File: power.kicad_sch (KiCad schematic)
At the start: 45 parts, among them J501 PJ-002AH-SMT-TR, Q501 SI2369DS-T1-BE3, U501 TPS5402, U502 TLV1117-50, U503 MIC5317-3.3YM5-TR

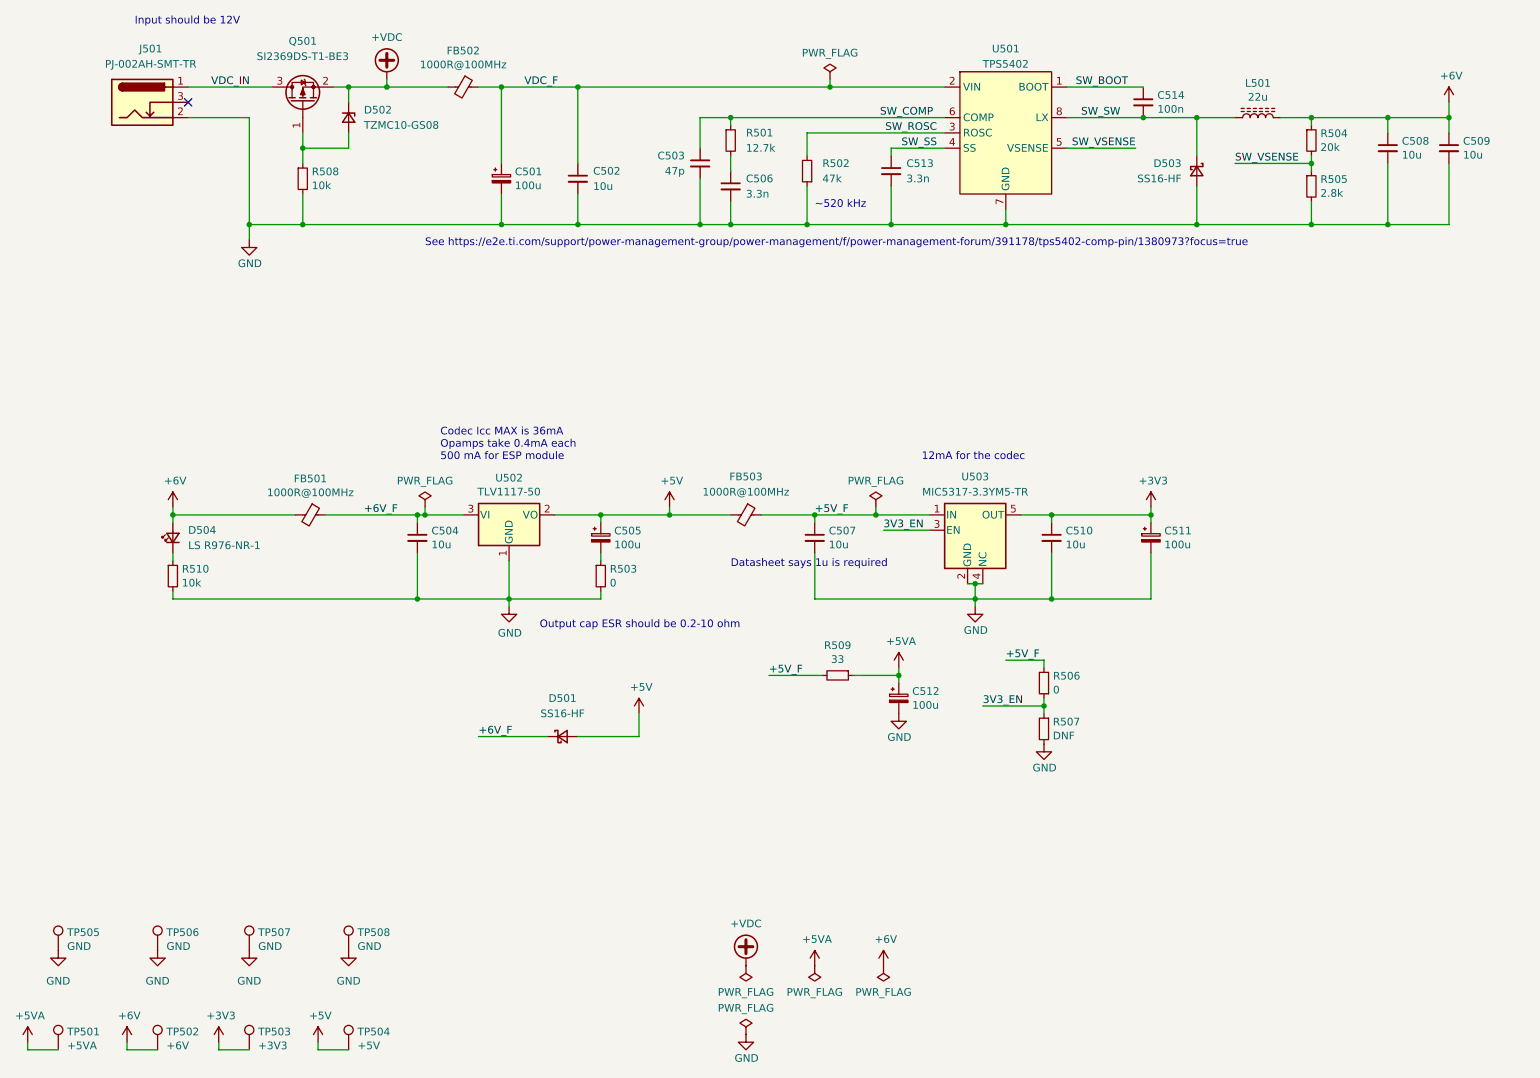
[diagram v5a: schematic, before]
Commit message: Resolve some issues
- Add missing MIDI connector pins to symbol
- Isolate low-ESR capacitors from 1117
- Fix DRC errors in footprints
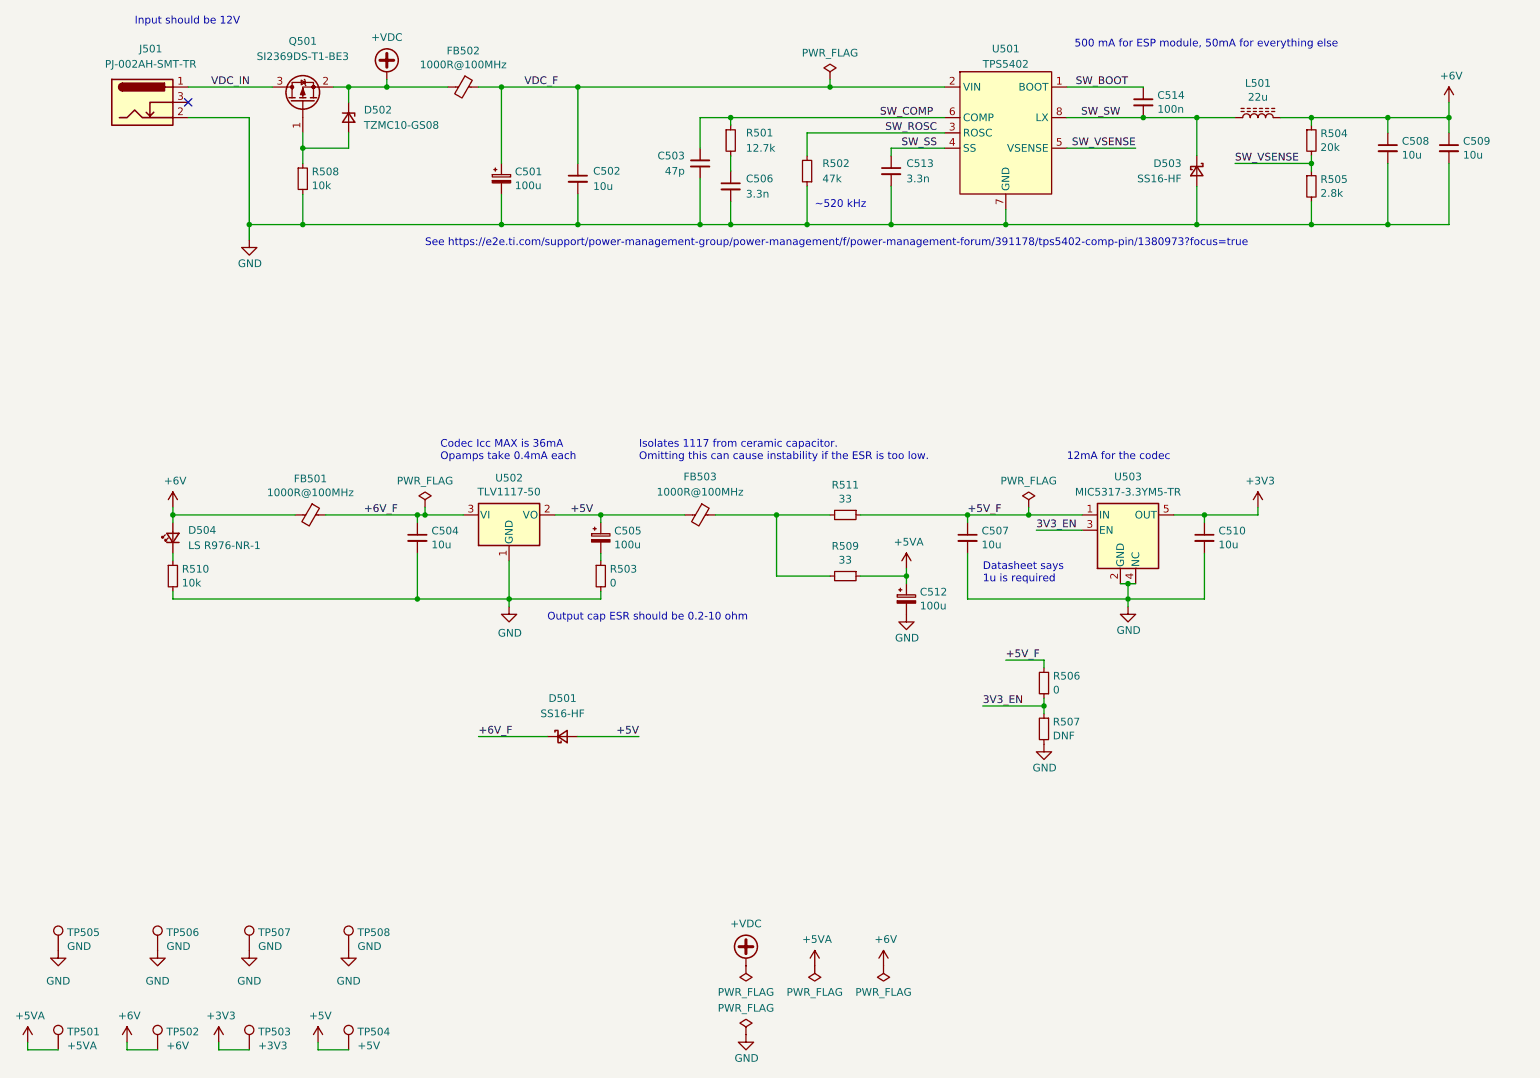
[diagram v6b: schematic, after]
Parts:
- removed C511: 100u, Capacitor_SMD:CP_Elec_6.3x7.7, symbol Device:CP_Small
- added R511: 33, Resistor_SMD:R_0805_2012Metric_Pad1.20x1.40mm_HandSolder, symbol Device:R_Small
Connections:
- net +5V_F: now also R511.1; no longer FB503.1, R509.2
- new net: FB503.1, R509.2, R511.2
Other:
- note added: "500 mA for ESP module, 50mA for everything else"
- note added: "Codec Icc MAX is 36mA Opamps take 0.4mA each"
- note added: "Isolates 1117 from ceramic capacitor. Omitting this can cause instability if the ESR is too low."
- note removed: "Codec Icc MAX is 36mA Opamps take 0.4mA each 500 mA for ESP module"
- moved on the sheet: C507, C510, C512, FB503, R509, U503

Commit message: Fix incorrect part number
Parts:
- R502: PN CR0805-FX-2002ELF -> CR0805-FX-4702ELF
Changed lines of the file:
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@@
       (effects (font (size 1.27 1.27)) hide)
     )
-    (property "PN" "CR0805-FX-2002ELF" (id 4) (at 153.67 44.45 0)
+    (property "PN" "CR0805-FX-4702ELF" (id 4) (at 153.67 44.45 0)
       (effects (font (size 1.27 1.27)) hide)
     )
